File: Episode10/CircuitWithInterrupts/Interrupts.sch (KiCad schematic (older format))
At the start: 15 parts, among them U401 74HCT74, U402 74HCT11, U403 74HCT147, U404 74HCT540

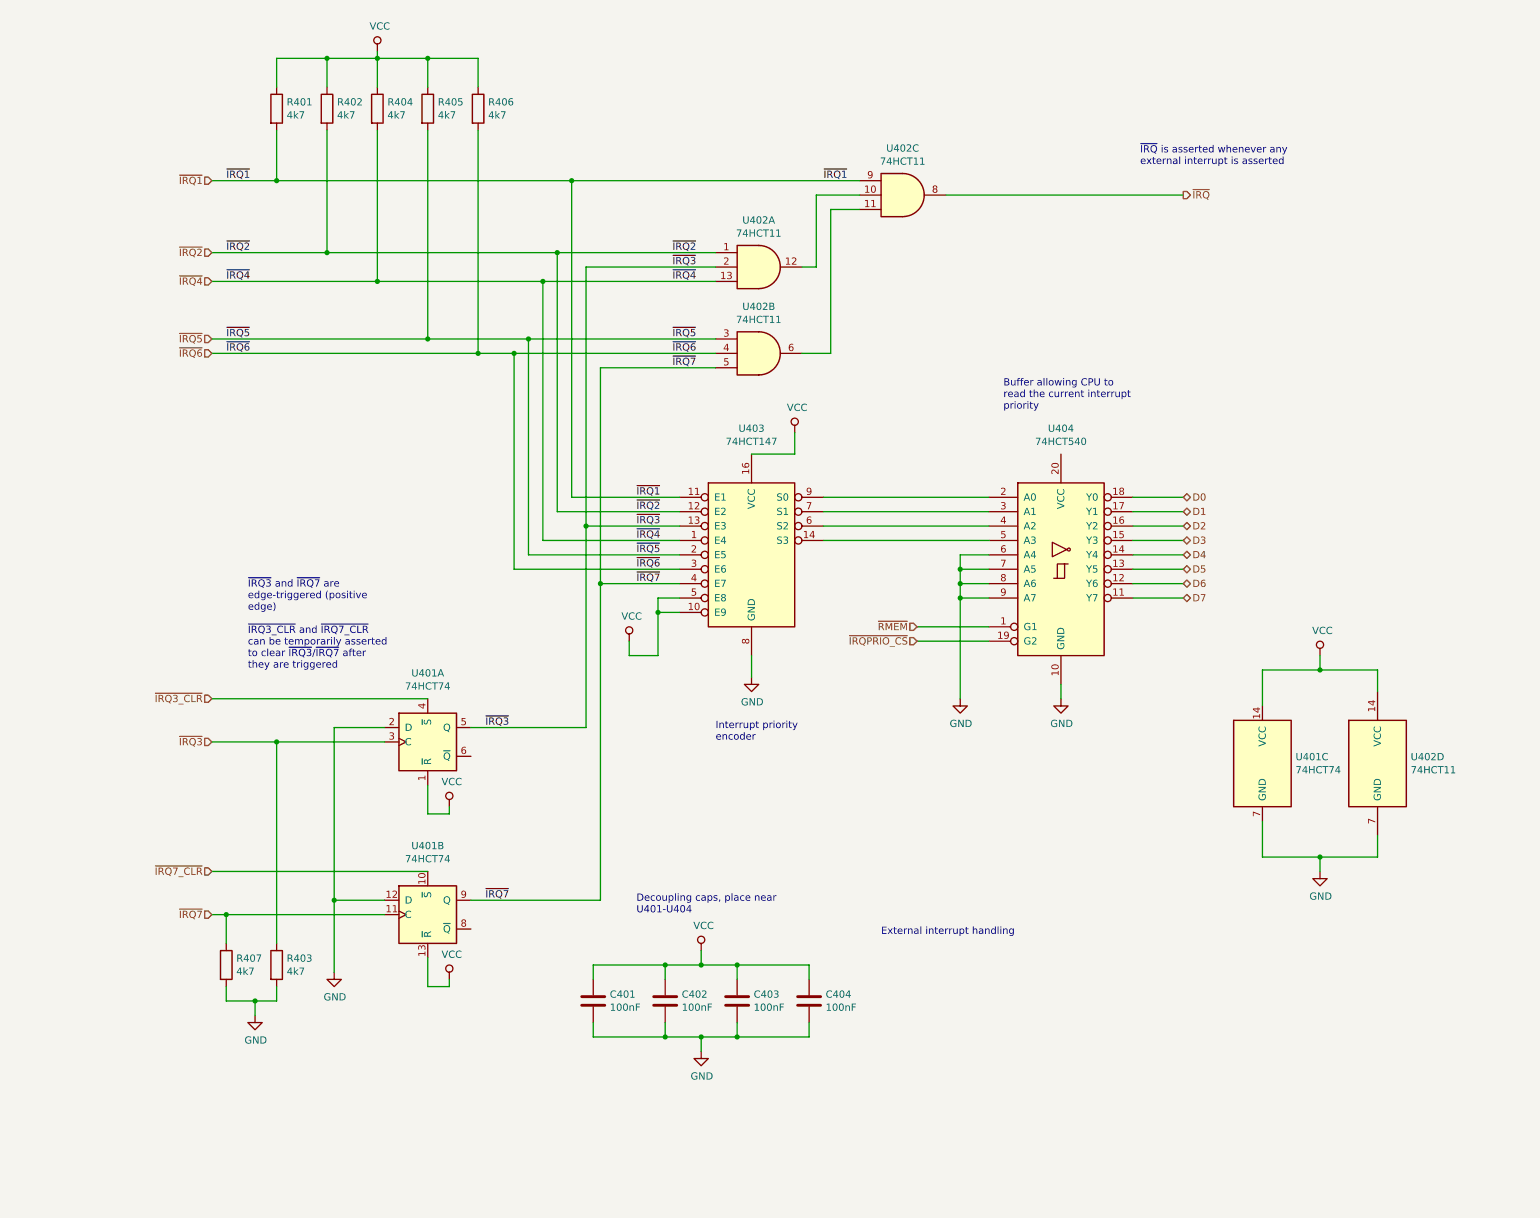
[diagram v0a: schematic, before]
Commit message: allow individual IRQs to be enabled and disabled
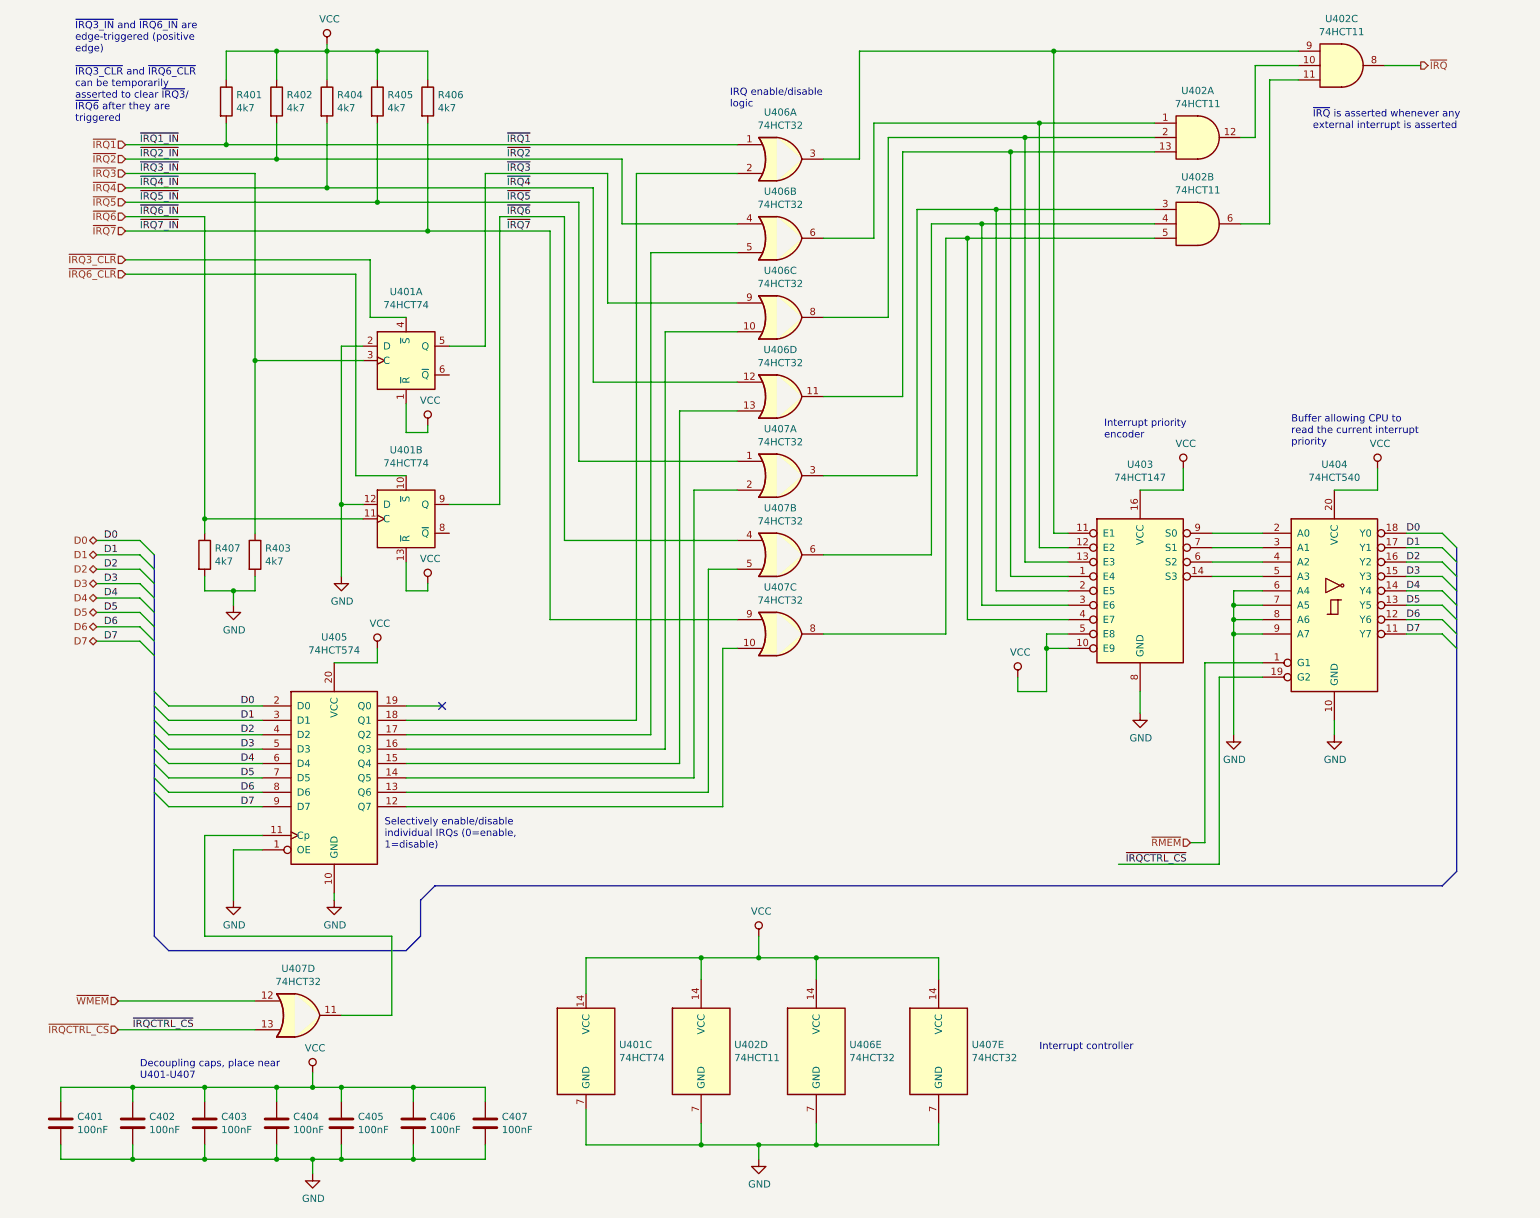
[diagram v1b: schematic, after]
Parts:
- added C405, C406, C407: 100nF, symbol device:C
- added U405: 74HCT574, symbol 74xx:74LS574
- added U406, U407: 74HCT32, symbol 74xx:74LS32
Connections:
- net D0: now also U405.2 (D0)
- net D1: now also U405.3 (D1)
- net D2: now also U405.4 (D2)
- net D3: now also U405.5 (D3)
- net D4: now also U405.6 (D4)
- net D5: now also U405.7 (D5)
- net D6: now also U405.8 (D6)
- net D7: now also U405.9 (D7)
- net GND: now also C405.2, C406.2, C407.2, U405.1 (OE), U405.10 (GND), U406.7 (GND), U407.7 (GND)
- net VCC: now also U404.20 (VCC), C405.1, C406.1, C407.1, U405.20 (VCC), U406.14 (VCC), U407.14 (VCC)
- net ~IRQ1: now also U406.1; no longer U402.9, U403.11 (E1)
- net ~IRQ2: now also U406.4; no longer U402.1, U403.12 (E2)
- net ~IRQ3: now also U406.9; no longer U402.2, U403.13 (E3)
- net ~IRQ4: now also U406.12; no longer U402.13, U403.1 (E4)
- net ~IRQ5: now also U407.1; no longer U402.3, U403.2 (E5)
- net ~IRQ6: now also R407.1, U401.11 (C), U401.9 (Q), U407.4; no longer R406.2, U402.4, U403.3 (E6)
- net ~IRQ7: now also R406.2, U407.9; no longer R407.1, U401.11 (C), U401.9 (Q), U402.5, U403.4 (E7)
- net ~IRQ7_CLR renamed ~IRQ6_CLR
- net ~IRQPRIO_CS renamed ~IRQCTRL_CS
- net ~IRQCTRL_CS: now also U407.13
- new net: U402.13, U403.1 (E4), U406.11
- new net: U402.9, U403.11 (E1), U406.3
- new net: U402.1, U403.12 (E2), U406.6
- new net: U402.2, U403.13 (E3), U406.8
- new net: U402.3, U403.2 (E5), U407.3
- new net: U402.4, U403.3 (E6), U407.6
- new net: U402.5, U403.4 (E7), U407.8
- new net: U405.11 (Cp), U407.11
- new net: U405.12 (Q7), U407.10
- new net: U405.13 (Q6), U407.5
- new net: U405.14 (Q5), U407.2
- new net: U405.15 (Q4), U406.13
- new net: U405.16 (Q3), U406.10
- new net: U405.17 (Q2), U406.5
- new net: U405.18 (Q1), U406.2
- new net ~WMEM: U407.12
- no-connect marks 0 -> 1
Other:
- note added: "Decoupling caps, place near\nU401-U407"
- note added: "IRQ enable/disable\nlogic"
- note added: "Interrupt controller"
- note added: "Selectively enable/disable\nindividual IRQs (0=enable,\n1=disable)"
- note added: "~IRQ3_IN~ and ~IRQ6_IN~ are\nedge-triggered (positive\nedge)\n\n~IRQ3_CLR~ and ~IRQ6_CLR~\ncan be temporarily\nasserted to clear ~IRQ3~/\n~IRQ6~ after they are\ntriggered"
- note removed: "Decoupling caps, place near\nU401-U404"
- note removed: "External interrupt handling"
- note removed: "~IRQ3~ and ~IRQ7~ are\nedge-triggered (positive\nedge)\n\n~IRQ3_CLR~ and ~IRQ7_CLR~\ncan be temporarily asserted\nto clear ~IRQ3~/~IRQ7~ after\nthey are triggered"
- moved on the sheet: C401, C402, C403, C404, R401, R402, R403, R404, R405, R406, R407, U401A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
